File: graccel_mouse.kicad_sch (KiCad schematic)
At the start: 17 parts

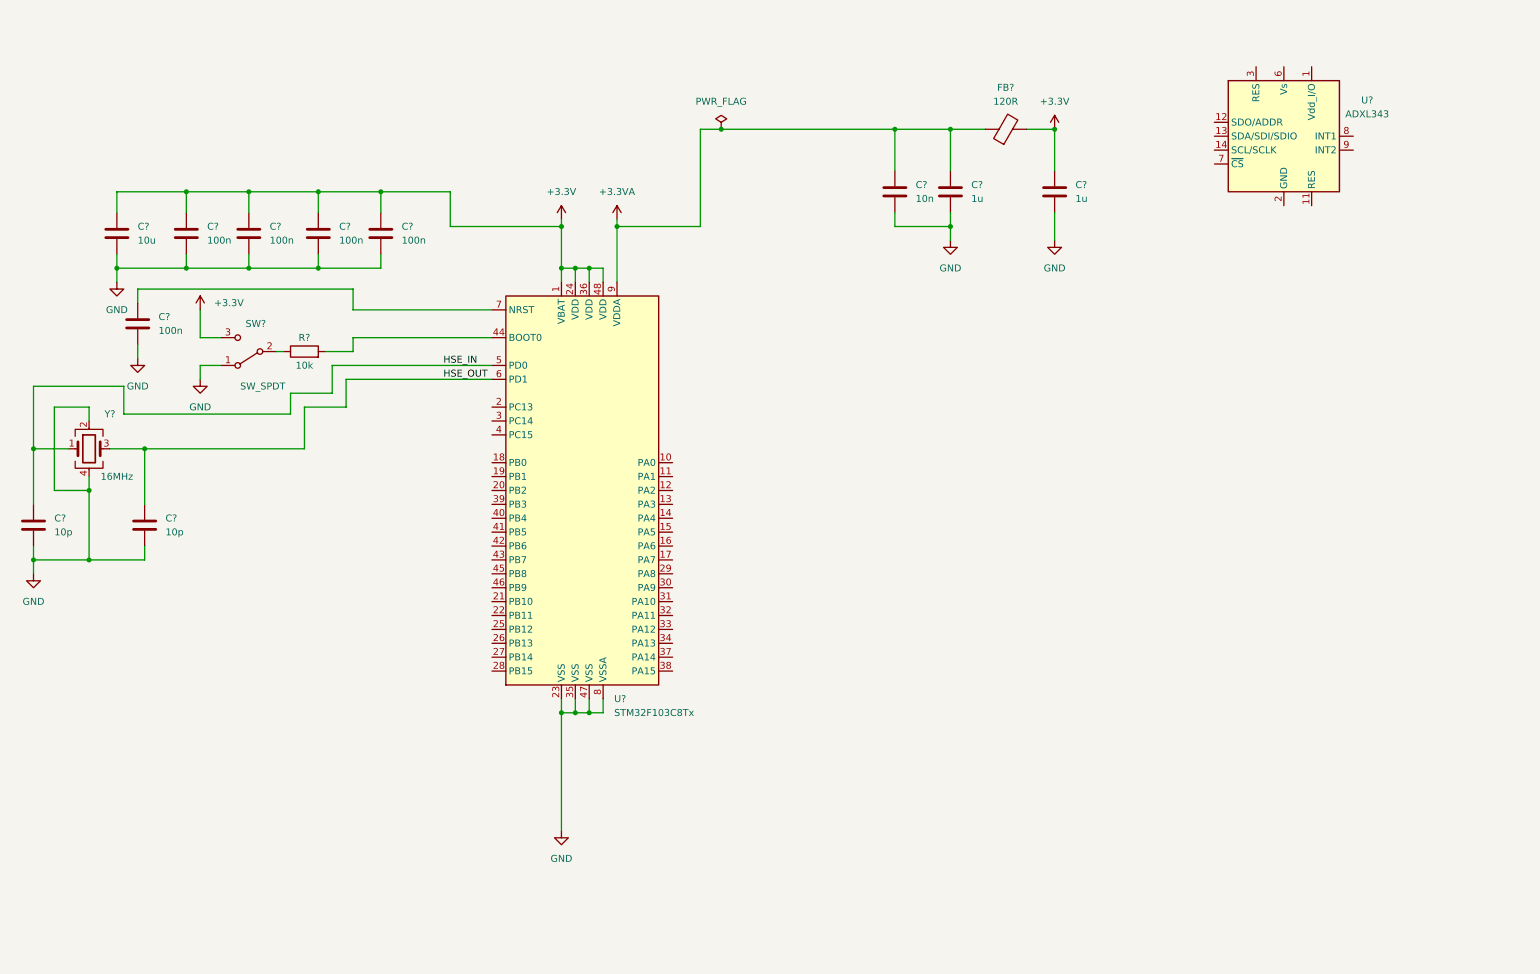
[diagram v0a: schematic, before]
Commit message: complete mouse with button
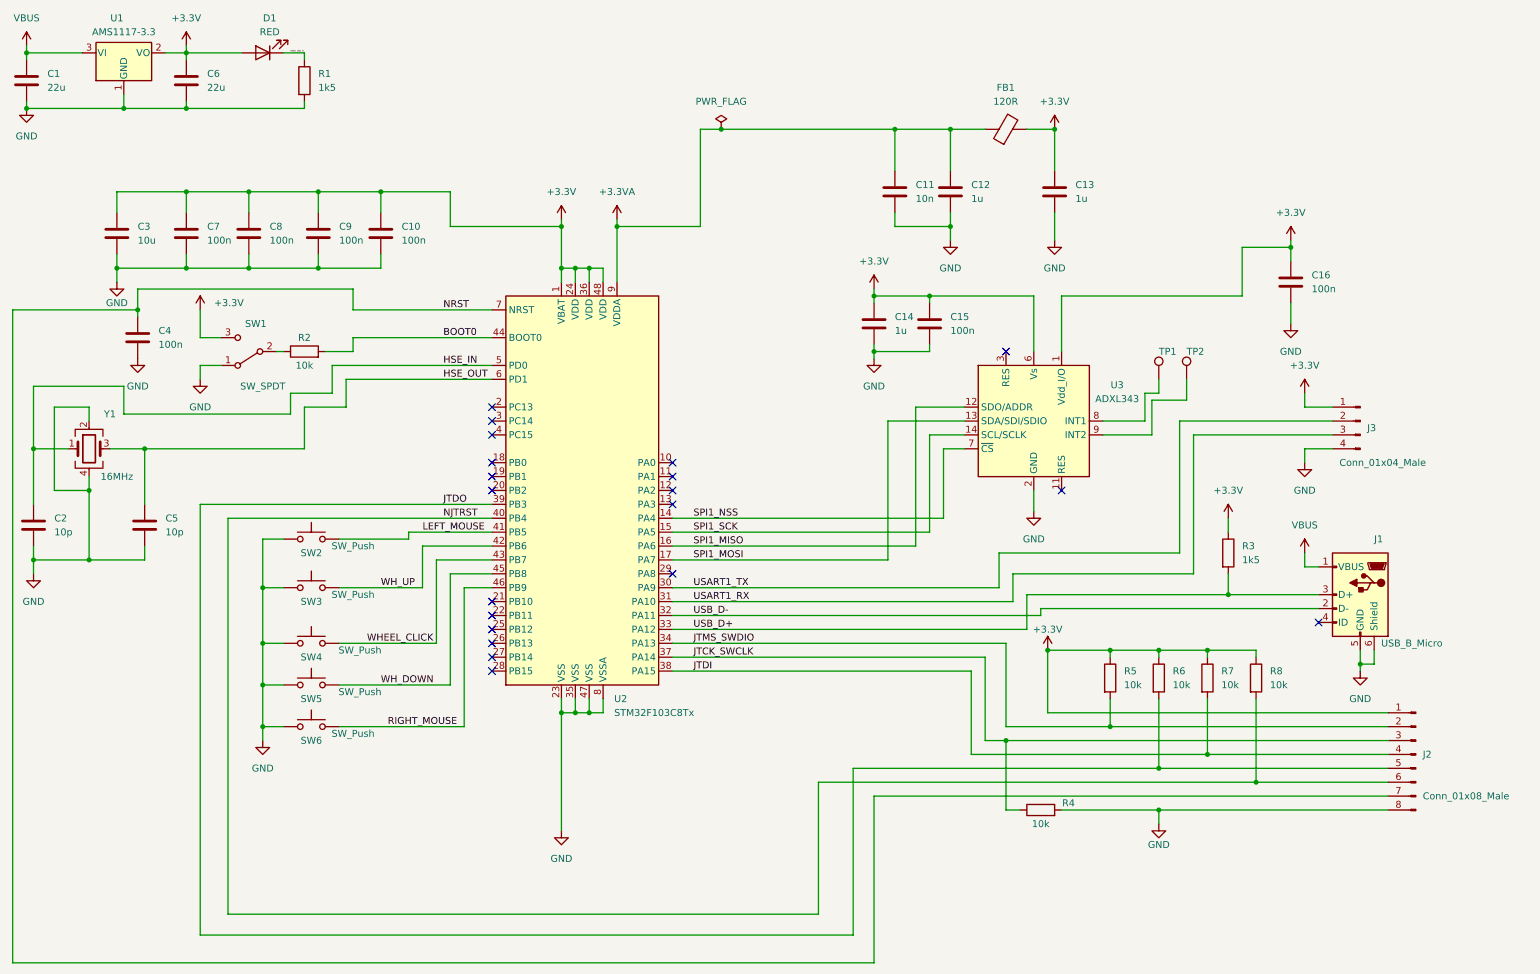
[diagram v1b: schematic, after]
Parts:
- added C1, C6: 22u, Capacitor_SMD:C_0805_2012Metric, symbol Device:C
- added C14: 1u, Capacitor_SMD:C_0402_1005Metric, symbol Device:C
- added C15, C16: 100n, Capacitor_SMD:C_0402_1005Metric, symbol Device:C
- added D1: RED, LED_SMD:LED_0603_1608Metric, symbol Device:LED
- added J1: USB_B_Micro, Connector_USB:USB_Micro-B_Wuerth_629105150521, symbol Connector:USB_B_Micro
- added J2: Conn_01x08_Male, Connector_PinHeader_2.54mm:PinHeader_1x08_P2.54mm_Vertical, symbol Connector:Conn_01x08_Male
- added J3: Conn_01x04_Male, Connector_PinHeader_2.54mm:PinHeader_1x04_P2.54mm_Vertical, symbol Connector:Conn_01x04_Male
- added R1, R3: 1k5, Resistor_SMD:R_0402_1005Metric, symbol Device:R
- added R4, R5, R6, R7, R8: 10k, Resistor_SMD:R_0402_1005Metric, symbol Device:R
- added SW2, SW3, SW4, SW5, SW6: SW_Push, Button_Switch_THT:SW_PUSH_6mm, symbol Switch:SW_Push
- added TP1, TP2: TestPoint, TestPoint:TestPoint_Pad_D1.0mm, symbol Connector:TestPoint
- added U1: AMS1117-3.3, Package_TO_SOT_SMD:SOT-223-3_TabPin2, symbol Regulator_Linear:AMS1117-3.3
- C10, C11, C12, C13, C2, C4, C5, C7, C8, C9: renamed from C?; footprint (none) -> Capacitor_SMD:C_0402_1005Metric
- C3: renamed from C?; footprint (none) -> Capacitor_SMD:C_0603_1608Metric
- FB1: renamed from FB?; footprint (none) -> Inductor_SMD:L_0603_1608Metric
- R2: renamed from R?; footprint (none) -> Resistor_SMD:R_0402_1005Metric
- SW1: renamed from SW?; footprint (none) -> Button_Switch_SMD:SW_SPDT_PCM12
- Y1: renamed from Y?; footprint (none) -> Crystal:Crystal_SMD_3225-4Pin_3.2x2.5mm
- gave numbers to parts that had none: 2
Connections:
- net +3.3V: now also U3.1 (Vdd_I/O), U3.6 (Vs), C14.1, C15.1, C16.1, C6.1, D1.2 (A), J2.1 (Pin_1), J3.1 (Pin_1), R3.1, R5.1, R6.1, R7.1, R8.1, U1.2 (VO)
- net GND: now also U3.2 (GND), U3.4 (GND), U3.5 (GND), C1.2, C14.2, C15.2, C16.2, C6.2, J1.5 (GND), J1.6 (Shield), J2.8 (Pin_8), J3.4 (Pin_4), R1.2, R4.2, SW2.1, SW3.1, SW4.1, SW5.1, SW6.1, U1.1 (GND)
- net BOOT0: now reaches R2.2, U2.44 (BOOT0)
- net NRST: now reaches C4.1, U2.7 (NRST)
- net NRST: now also J2.7 (Pin_7)
- net SPI1_NSS: now reaches U2.14 (PA4)
- net SPI1_NSS: now also U3.7 (~{CS})
- net SPI1_SCK: now reaches U2.15 (PA5)
- net SPI1_SCK: now also U3.14 (SCL/SCLK)
- net SPI1_MISO: now reaches U2.16 (PA6)
- net SPI1_MISO: now also U3.12 (SDO/ADDR)
- net SPI1_MOSI: now reaches U2.17 (PA7)
- net SPI1_MOSI: now also U3.13 (SDA/SDI/SDIO)
- net USART1_TX: now reaches U2.30 (PA9)
- net USART1_TX: now also J3.2 (Pin_2)
- net USART1_RX: now reaches U2.31 (PA10)
- net USART1_RX: now also J3.3 (Pin_3)
- net USB_D-: now reaches U2.32 (PA11)
- net USB_D-: now also J1.2 (D-)
- net USB_D+: now reaches U2.33 (PA12)
- net USB_D+: now also J1.3 (D+), R3.2
- net JTMS_SWDIO: now reaches U2.34 (PA13)
- net JTMS_SWDIO: now also J2.2 (Pin_2), R5.2
- net JTCK_SWCLK: now reaches U2.37 (PA14)
- net JTCK_SWCLK: now also J2.3 (Pin_3), R4.1
- net JTDI: now reaches U2.38 (PA15)
- net JTDI: now also J2.4 (Pin_4), R7.2
- net JTDO: now reaches U2.39 (PB3)
- net JTDO: now also J2.5 (Pin_5), R6.2
- net NJTRST: now reaches U2.40 (PB4)
- net NJTRST: now also J2.6 (Pin_6), R8.2
- net LEFT_MOUSE: now reaches U2.41 (PB5)
- net LEFT_MOUSE: now also SW2.2
- net WH_UP: now reaches U2.42 (PB6)
- net WH_UP: now also SW3.2
- net WHEEL_CLICK: now reaches U2.43 (PB7)
- net WHEEL_CLICK: now also SW4.2
- net WH_DOWN: now reaches U2.45 (PB8)
- net WH_DOWN: now also SW5.2
- net RIGHT_MOUSE: now reaches U2.46 (PB9)
- net RIGHT_MOUSE: now also SW6.2
- net at U3.8 (INT1): now also TP1.1
- net at U3.9 (INT2): now also TP2.1
- new net PWR_LED_K: D1.1 (K), R1.1
- new net VBUS: C1.1, J1.1 (VBUS), U1.3 (VI)
- no-connect marks 0 -> 20
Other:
- moved on the sheet: C4, U3

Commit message: complete pcb design and add gerber, bom and cpl
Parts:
- J1: footprint Connector_USB:USB_Micro-B_Wuerth_629105150521 -> Connector_USB:USB_Micro-B_Molex_47346-0001
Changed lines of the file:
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@@
       (effects (font (size 1.27 1.27)) (justify right))
     )
-    (property "Footprint" "Connector_USB:USB_Micro-B_Wuerth_629105150521" (id 2) (at 256.54 120.65 0)
+    (property "Footprint" "Connector_USB:USB_Micro-B_Molex_47346-0001" (id 2) (at 256.54 120.65 0)
       (effects (font (size 1.27 1.27)) hide)
     )
@@
     )
     (path "/2ac05af4-47c3-4f40-a6cd-c2ab35e2388b"
-      (reference "J1") (unit 1) (value "USB_B_Micro") (footprint "Connector_USB:USB_Micro-B_Wuerth_629105150521")
+      (reference "J1") (unit 1) (value "USB_B_Micro") (footprint "Connector_USB:USB_Micro-B_Molex_47346-0001")
     )
     (path "/cb370592-4c62-48a6-8f61-446924da7035"
